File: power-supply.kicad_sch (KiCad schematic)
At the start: 1 part, among them U2 L78L05_SOT89

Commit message: added filter ckt, passes ERC, bumped to v0.2, ready for board layout
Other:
- title: (none) -> switched bandpass filter
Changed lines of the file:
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@@
 (kicad_sch (version 20230121) (generator eeschema)
-  (paper "A4")
+  (paper "USLetter")
+  (title_block
+    (title "switched bandpass filter")
+    (date "2023-07-20")
+    (rev "v0.2")
+    (comment 1 "Copyright © 2023 WA7GIL")
+  )
   (wire (pts (xy 109.22 71.12) (xy 109.22 77.47))
     (stroke (width 0) (type default))

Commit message: v0.2 passes ERC & DRC except for no solder mask between pads on SOT89
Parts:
- U2: footprint Package_TO_SOT_SMD:SOT-89-3 -> Package_TO_SOT_SMD:SOT-89-3_Handsoldering
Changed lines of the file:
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@@
       (effects (font (size 1.27 1.27)) (justify left))
     )
-    (property "Footprint" "Package_TO_SOT_SMD:SOT-89-3" (at 114.3 63.5 0)
+    (property "Footprint" "Package_TO_SOT_SMD:SOT-89-3_Handsoldering" (at 114.3 63.5 0)
       (effects (font (size 1.27 1.27) italic) hide)
     )

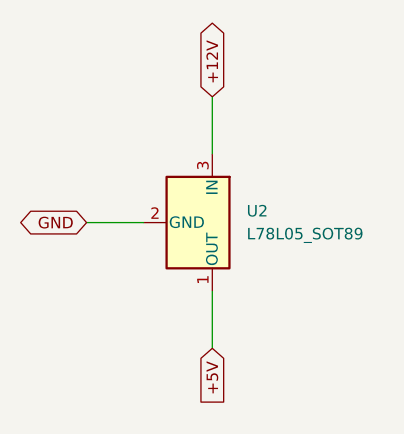
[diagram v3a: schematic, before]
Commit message: v0.4 ERC/DRC pass; added missing caps; mounting holes; moved SMA & headers out and re-spaced filter chains
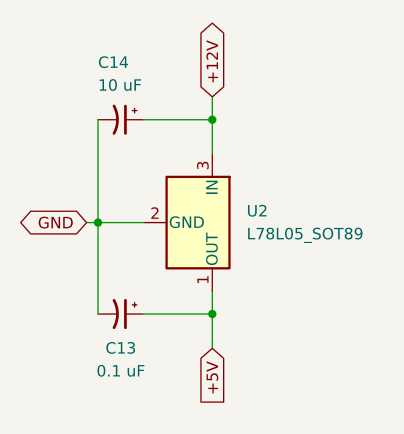
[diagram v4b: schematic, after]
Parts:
- added C13: 0.1 uF, Capacitor_SMD:C_1210_3225Metric, symbol Device:C_Polarized_Small_US
- added C14: 10 uF, Capacitor_SMD:C_1210_3225Metric, symbol Device:C_Polarized_Small_US
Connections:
- net +12V: now also C14.1
- net +5V: now also C13.1
- net GND: now also C13.2, C14.2
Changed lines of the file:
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@@
     (title "switched bandpass filter")
     (date "2023-07-22")
-    (rev "v0.3")
+    (rev "v0.4")
     (comment 1 "Copyright © 2023 WA7GIL")
   )
-  (wire (pts (xy 109.22 71.12) (xy 109.22 77.47))
+  (junction (at 109.22 73.66) (diameter 0) (color 0 0 0 0)
+  )
+  (junction (at 109.22 52.07) (diameter 0) (color 0 0 0 0)
+  )
+  (junction (at 96.52 63.5) (diameter 0) (color 0 0 0 0)
+  )
+  (wire (pts (xy 109.22 71.12) (xy 109.22 73.66))
     (stroke (width 0) (type default))
   )
-  (wire (pts (xy 109.22 49.53) (xy 109.22 55.88))
+  (wire (pts (xy 109.22 52.07) (xy 109.22 55.88))
     (stroke (width 0) (type default))
   )
-  (wire (pts (xy 95.25 63.5) (xy 101.6 63.5))
+  (wire (pts (xy 109.22 73.66) (xy 109.22 77.47))
+    (stroke (width 0) (type default))
+  )
+  (wire (pts (xy 109.22 49.53) (xy 109.22 52.07))
+    (stroke (width 0) (type default))
+  )
+  (wire (pts (xy 95.25 63.5) (xy 96.52 63.5))
+    (stroke (width 0) (type default))
+  )
+  (wire (pts (xy 101.6 73.66) (xy 109.22 73.66))
+    (stroke (width 0) (type default))
+  )
+  (wire (pts (xy 96.52 63.5) (xy 101.6 63.5))
+    (stroke (width 0) (type default))
+  )
+  (wire (pts (xy 96.52 63.5) (xy 96.52 73.66))
+    (stroke (width 0) (type default))
+  )
+  (wire (pts (xy 101.6 52.07) (xy 109.22 52.07))
+    (stroke (width 0) (type default))
+  )
+  (wire (pts (xy 96.52 52.07) (xy 96.52 63.5))
     (stroke (width 0) (type default))
   )
@@
         )
       )
+    )
+  )
+  (symbol (lib_id "Device:C_Polarized_Small_US") (at 99.06 52.07 270) (unit 1)
+    (in_bom yes) (on_board yes) (dnp no)
+    (property "Reference" "C14" (at 96.52 45.72 90)
+      (effects (font (size 1.27 1.27)) (justify left))
+    )
+    (property "Value" "10 uF" (at 96.52 48.26 90)
+      (effects (font (size 1.27 1.27)) (justify left))
+    )
+    (property "Footprint" "Capacitor_SMD:C_1210_3225Metric" (at 99.06 52.07 0)
+      (effects (font (size 1.27 1.27)) hide)
+    )
+    (property "Datasheet" "~" (at 99.06 52.07 0)
+      (effects (font (size 1.27 1.27)) hide)
+    )
+    (pin "1")
+    (pin "2")
+    (instances
+      (project "switched-bandpass-filter"
+        (path "/05f50450-de9a-44de-96d4-4a146d783d83/29c9003d-e0fe-43f3-aa63-0051569783eb"
+          (reference "C14") (unit 1)
+        )
+      )
+    )
+  )
+  (symbol (lib_id "Device:C_Polarized_Small_US") (at 99.06 73.66 270) (unit 1)
+    (in_bom yes) (on_board yes) (dnp no)
+    (property "Reference" "C13" (at 99.06 77.47 90)
+      (effects (font (size 1.27 1.27)))
+    )
+    (property "Value" "0.1 uF" (at 99.06 80.01 90)
+      (effects (font (size 1.27 1.27)))
+    )
+    (property "Footprint" "Capacitor_SMD:C_1210_3225Metric" (at 99.06 73.66 0)
+      (effects (font (size 1.27 1.27)) hide)
+    )
+    (property "Datasheet" "~" (at 99.06 73.66 0)
+      (effects (font (size 1.27 1.27)) hide)
+    )
+    (pin "1")
+    (pin "2")
+    (instances
+      (project "switched-bandpass-filter"
+        (path "/05f50450-de9a-44de-96d4-4a146d783d83/29c9003d-e0fe-43f3-aa63-0051569783eb"
+          (reference "C13") (unit 1)
+        )
+      )
